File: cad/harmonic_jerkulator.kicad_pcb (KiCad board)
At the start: 2 copper layers, 91 x 87 mm, 45 parts, among them J101 JACK_IN, J102 JACK_OUT, J103 CONN_PSU, J105 PNP, J106 NPN, J107 SW_BYPASS, J108 DIODE1, J109 DIODE_SW, J110 DIODE2, J111 Conn_01x06, J113 Conn_01x06, K101 TQ2SA-5V, Q101 BC850, Q102 BC856, Q103 DTC123Y, Q104 DTC123Y, Q105 DTA114E, U101 4013

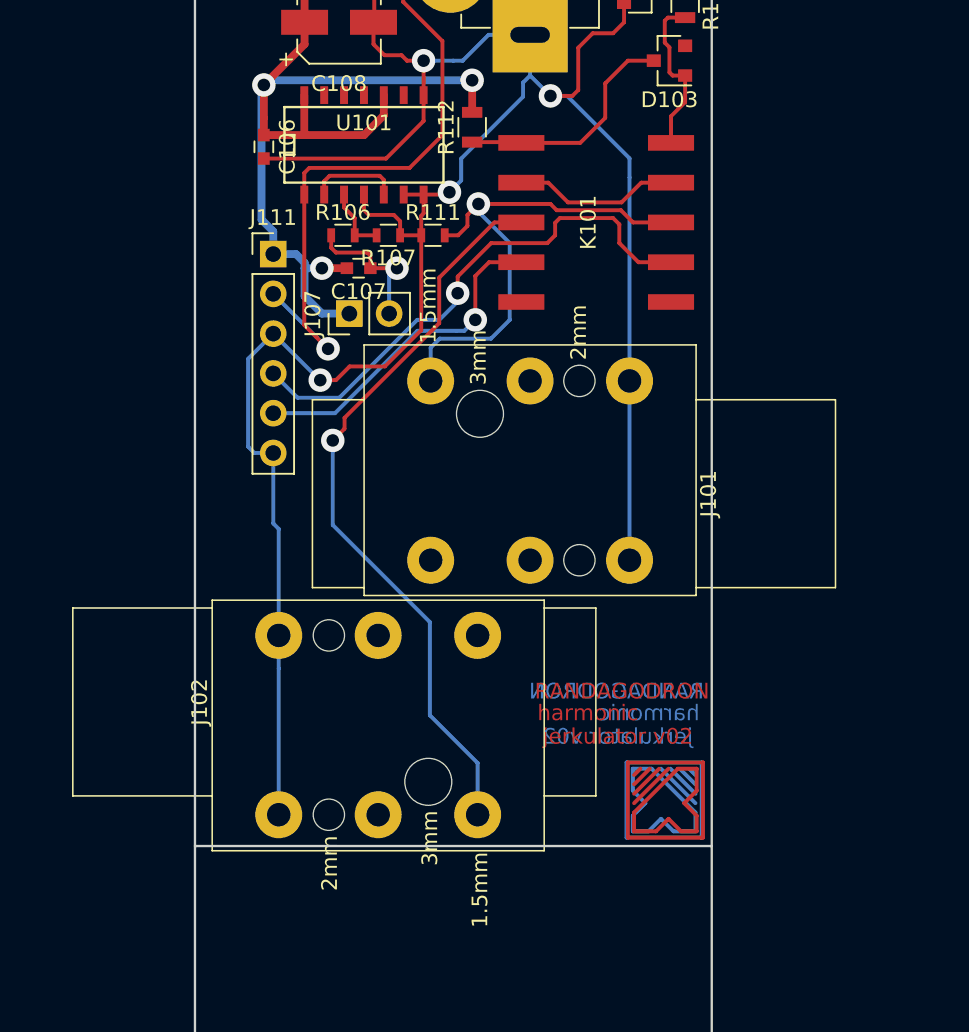
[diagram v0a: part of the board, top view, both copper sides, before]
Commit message: Corrected jacks spacing.
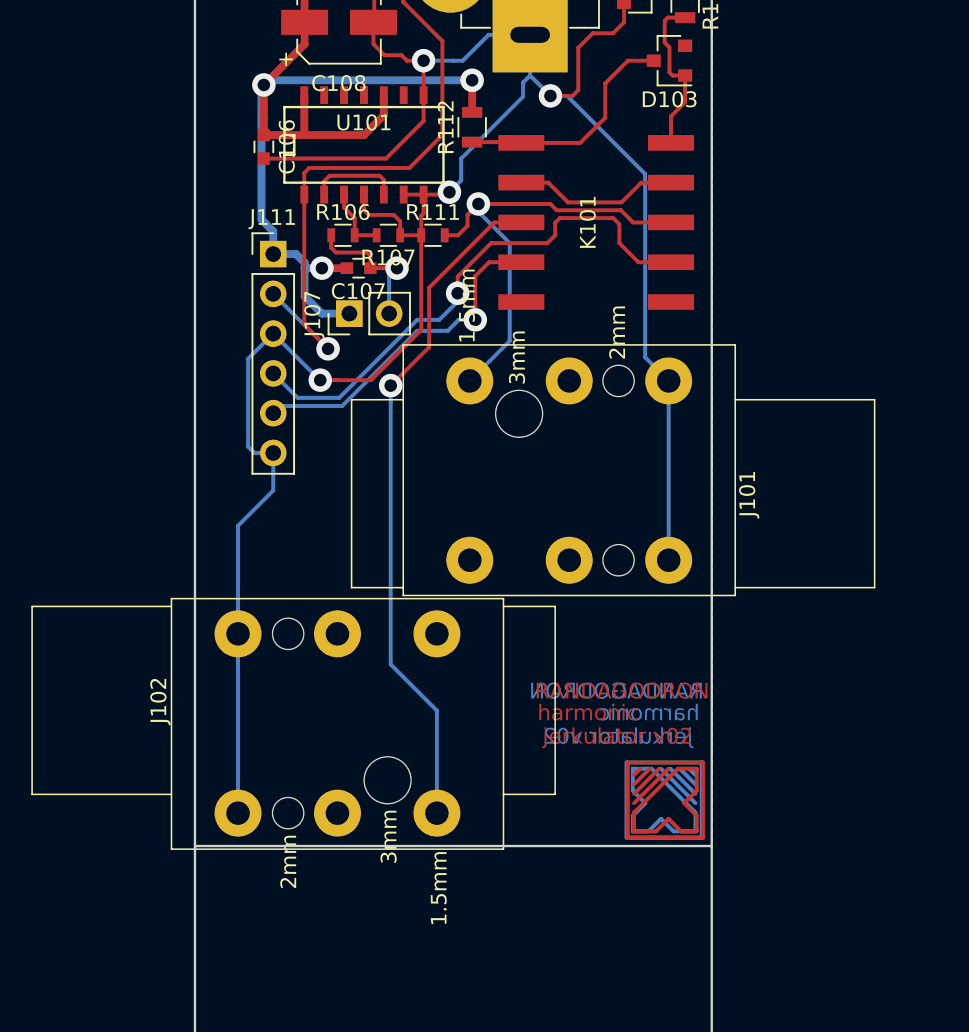
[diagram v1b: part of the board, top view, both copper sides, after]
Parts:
- moved J102 2.60 mm to (62.5, 100.7)
- moved J101 2.50 mm to (98.5, 87.5)
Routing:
- net /AUDIO_OUT: track 47.6 -> 43.4 mm
- net /AUDIO_IN: track 32.3 -> 29.4 mm
- net GND: track 154.3 -> 156.0 mm
